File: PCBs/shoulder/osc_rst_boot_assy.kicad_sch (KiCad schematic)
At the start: 8 parts, among them SW1 RESET

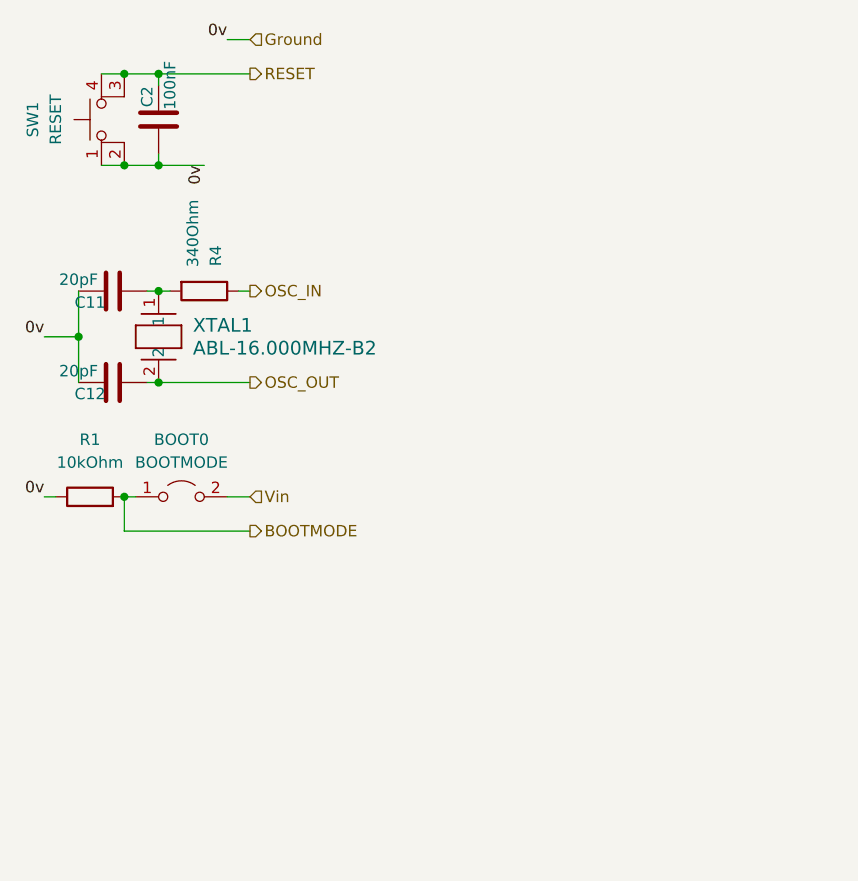
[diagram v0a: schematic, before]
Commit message: Torso all but complete, making bogie before checking the last mark
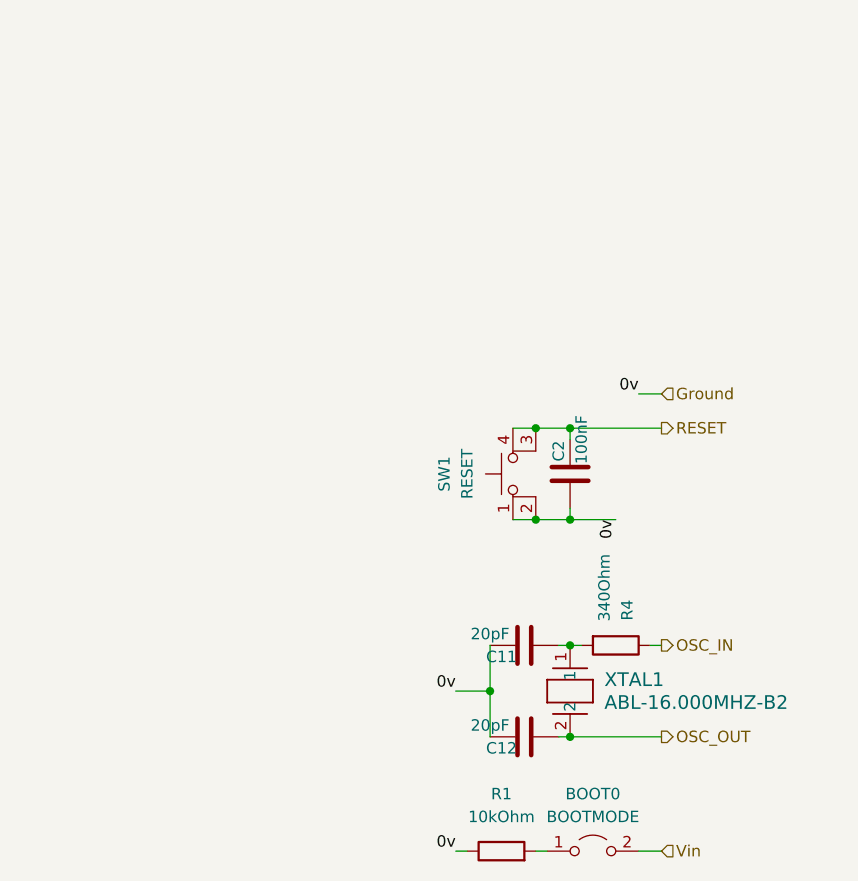
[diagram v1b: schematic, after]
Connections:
- net BOOTMODE: no longer names the net of BOOT0.1 (A), R1.2
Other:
- moved on the sheet: BOOT0, C11, C12, C2, R1, R4, SW1, XTAL1
